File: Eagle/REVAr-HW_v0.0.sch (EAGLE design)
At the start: 87 parts, among them IC1 MC33269ST-5.0T3, IC2 MC33269D-5.0, IC3 ATMEGA2560-16AU, IC4 ATMEGA8U2-MU, IC5 LM358D, IC6 LP2985-33DBVR, Q1 16MHz, Q2 16MHz, T2 FDN340P, X1 DC21MMX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

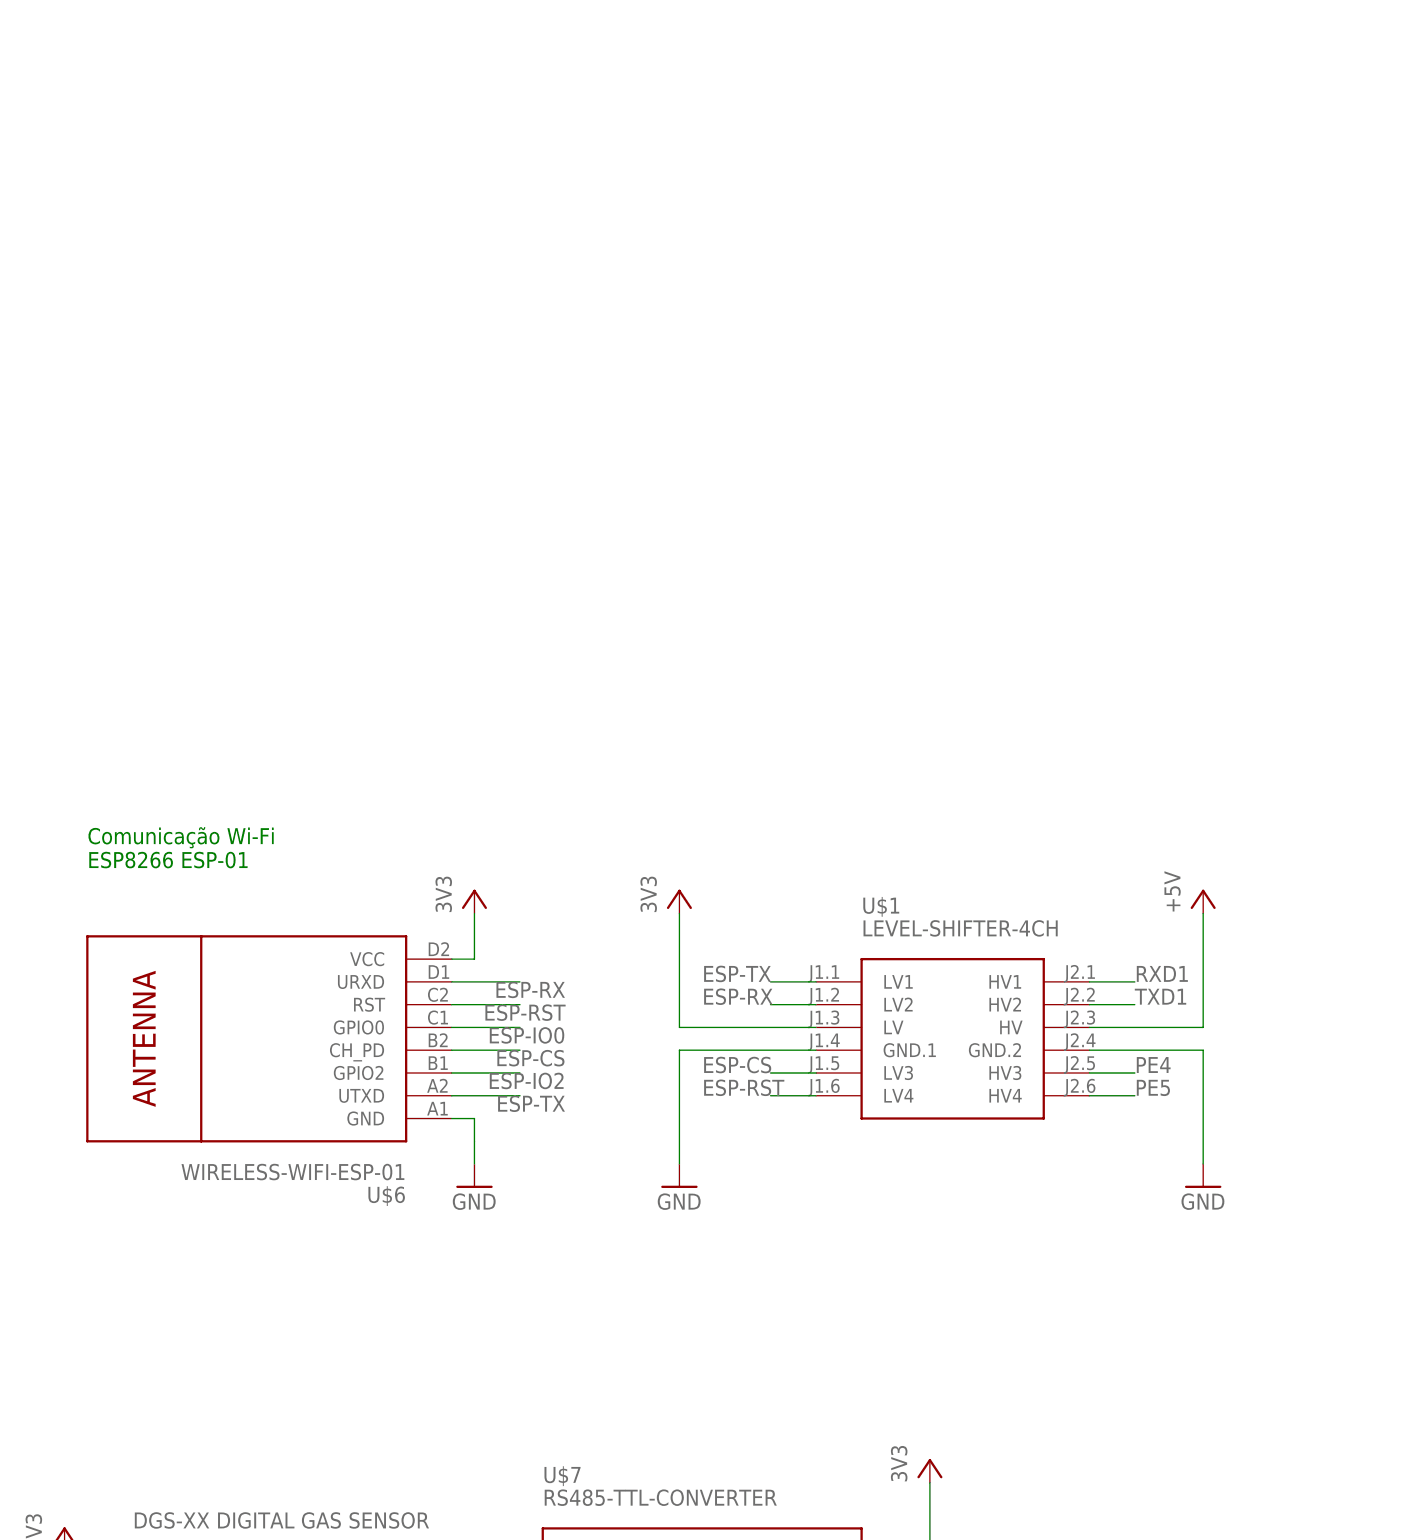
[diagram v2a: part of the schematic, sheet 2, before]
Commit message: [HW] Add PCF8574 I2C port expander for LCD Display
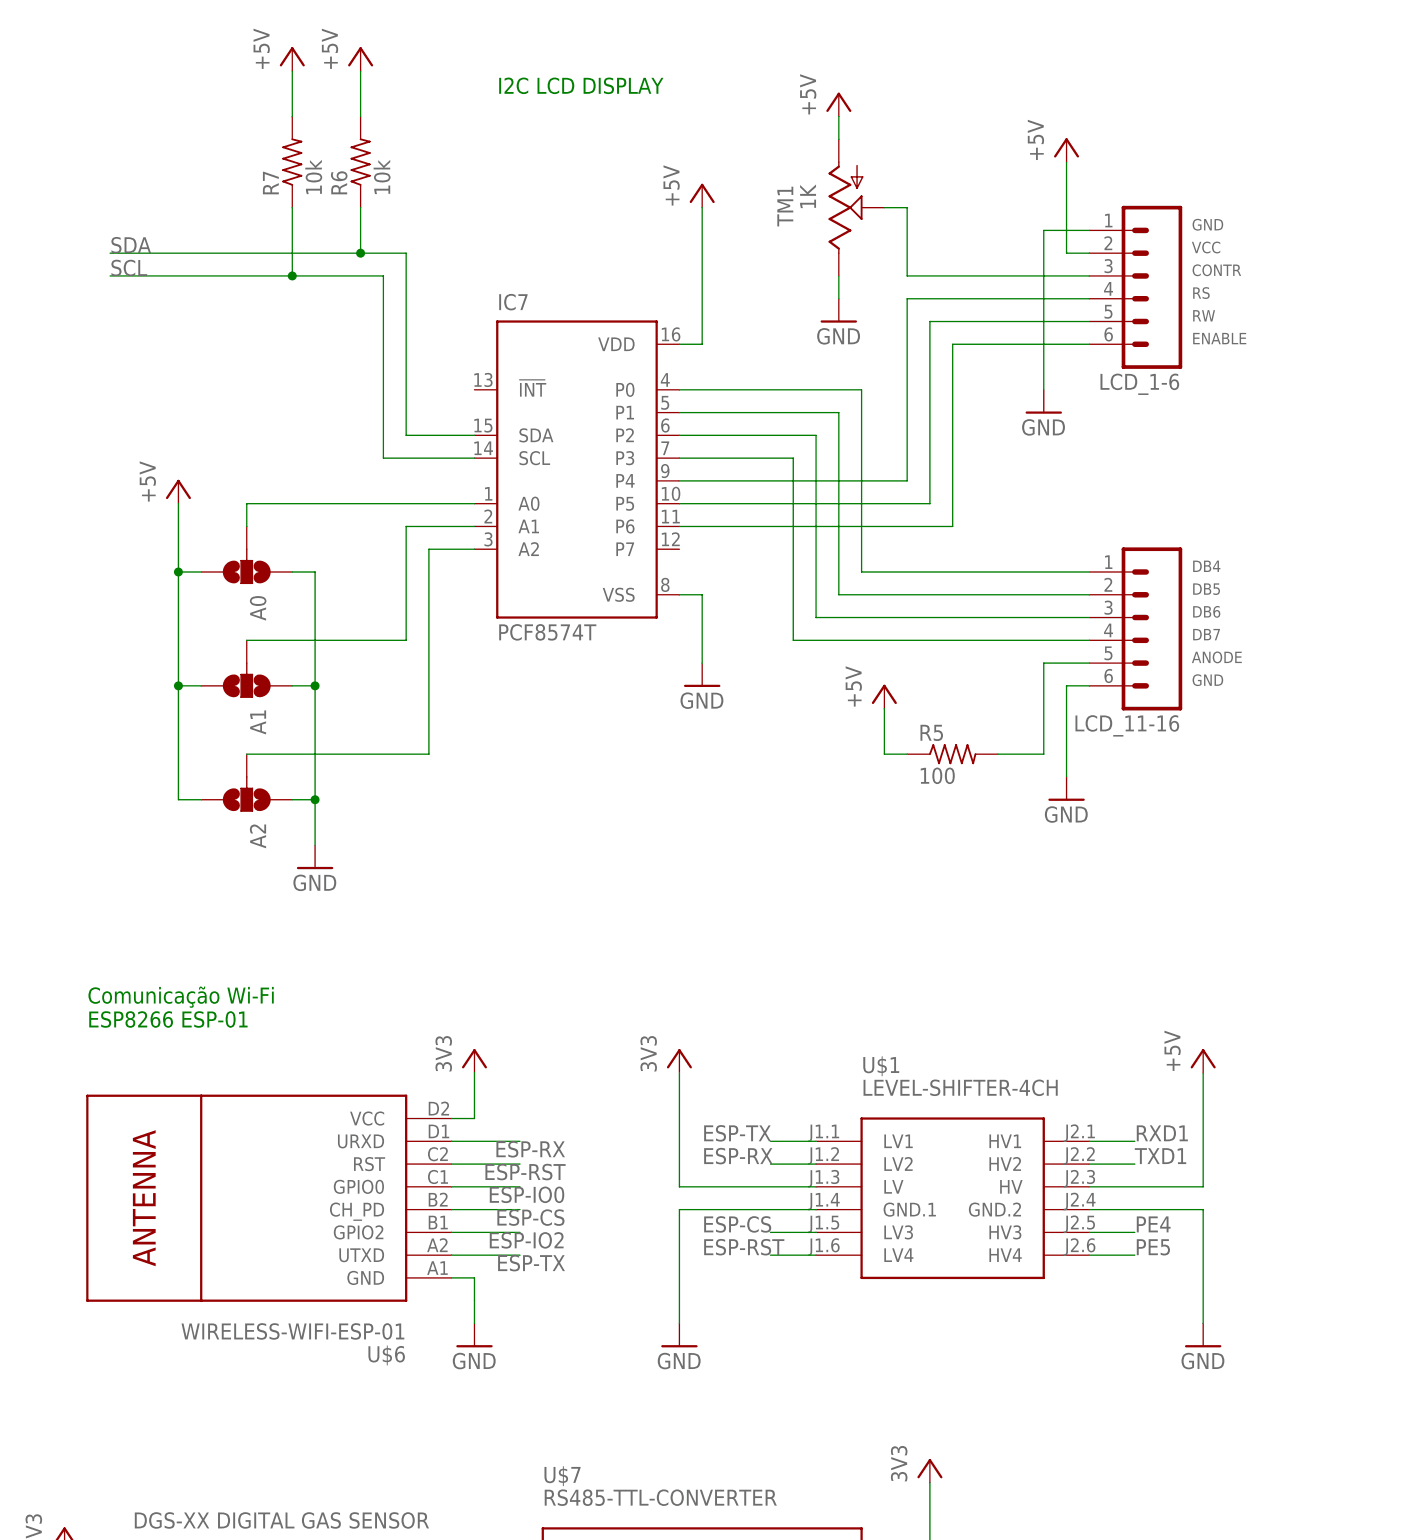
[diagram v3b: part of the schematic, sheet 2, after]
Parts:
- added A0, A1, A2: (no value), SparkFun:SOLDERJUMPER_2WAYT
- added IC7: PCF8574T, micro-philips:PCF8574T
- added LCD_1-6, LCD_11-16: (no value), SparkFun-Connectors:M06SIP
- added R5: 100, adafruit:R-US_R0805
- added R6, R7: 10k, adafruit:R-US_R0805
- added TM1: 1K, adafruit:TRIM
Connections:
- new net A0: A0.2, IC7.A0
- new net A1: A1.2, IC7.A1
- new net A2: A2.2, IC7.A2
- new net ANODE: LCD_11-16.5, R5.2
- new net CONTR: LCD_1-6.3, TM1.S
- new net DB4: IC7.P0, LCD_11-16.1
- new net DB5: IC7.P1, LCD_11-16.2
- new net DB6: IC7.P2, LCD_11-16.3
- new net DB7: IC7.P3, LCD_11-16.4
- new net ENABLE: IC7.P6, LCD_1-6.6
- new net RS: IC7.P4, LCD_1-6.4
- new net RW: IC7.P5, LCD_1-6.5
- net GND: now also A0.1, A1.1, A2.1, IC7.VSS, LCD_1-6.1, LCD_11-16.6, TM1.E
- net SCL: now also IC7.SCL, R7.1
- net SDA: now also IC7.SDA, R6.1
- net VCC: now also A0.3, A1.3, A2.3, IC7.VDD, LCD_1-6.2, R5.1, R6.2, R7.2, TM1.A
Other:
- note added: "I2C LCD DISPLAY"
- moved on the sheet: U$1, U$6
